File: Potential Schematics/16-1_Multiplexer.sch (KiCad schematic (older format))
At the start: 2 parts, among them U181 74LS04, U194 74LS04

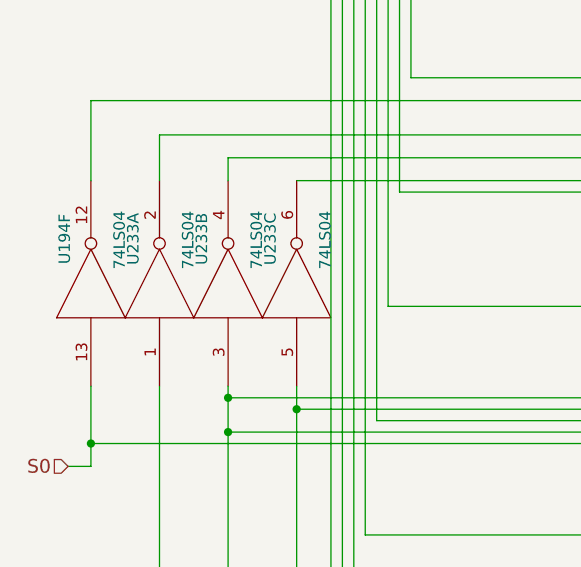
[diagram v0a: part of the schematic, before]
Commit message: Added Registers to Top Schematic
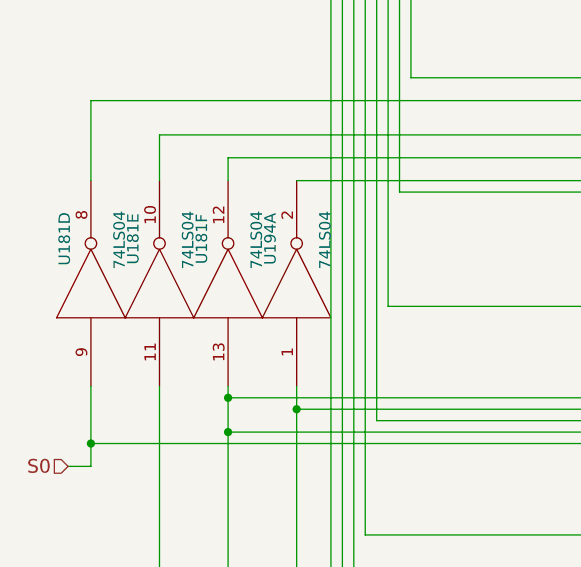
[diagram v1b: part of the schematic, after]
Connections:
- net 5:1_AND/b: now also U194.2; no longer U194.5
- net 5:1_AND/c: now also U181.13; no longer U181.3
- net 5:1_AND/d: now also U181.10; no longer U181.2
- net S0: now also U181.9; no longer U181.13
- net S1: now also U181.11; no longer U181.1
- removed net 5:1_AND/b: U194.6
- removed net 5:1_AND/c: U181.12, U181.4
- new net 5:1_AND/b: U194.1
- new net 5:1_AND/c: U181.12, U181.8
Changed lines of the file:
@@
 $Descr A4 11693 8268
 encoding utf-8
-Sheet 414 449
+Sheet 378 449
 Title "16:1 Multiplexer"
 Date "2018-09-14"
@@
 $Comp
 L 74LS04 U194
-U 3 1 5BB53D19
+U 1 1 5BB53D19
 P 1700 5450
 AR Path="/5B9D167A/5B9C0EA0/5BAE2F4B/5BAE3D50/5BB53D19" Ref="U194"  Part="1"
@@
 AR Path="/5B9D167A/5B9C0EA0/5BAE2F4B/5BC8F4EC/5BB53D19" Ref="U233"  Part="3"
 AR Path="/5B9D167A/5B9C0EA0/5BAE2F4B/5BC8F503/5BB53D19" Ref="U253"  Part="1"
-F 0 "U233" H 1895 5565 50  0000 C CNN
+F 0 "U194" H 1895 5565 50  0000 C CNN
 F 1 "74LS04" H 1890 5325 50  0000 C CNN
 F 2 "" H 1700 5450 50  0001 C CNN
 F 3 "" H 1700 5450 50  0001 C CNN
-	3    1700 5450
+	1    1700 5450
 	0    -1   -1   0
 $EndComp
 $Comp
 L 74LS04 U181
-U 2 1 5BB54417
+U 6 1 5BB54417
 P 1400 5450
 AR Path="/5B9D167A/5B9C0EA0/5BAE2F4B/5BAE3D50/5BB54417" Ref="U181"  Part="6"
@@
 AR Path="/5B9D167A/5B9C0EA0/5BAE2F4B/5BC8F4EC/5BB54417" Ref="U233"  Part="2"
 AR Path="/5B9D167A/5B9C0EA0/5BAE2F4B/5BC8F503/5BB54417" Ref="U233"  Part="6"
-F 0 "U233" H 1595 5565 50  0000 C CNN
+F 0 "U181" H 1595 5565 50  0000 C CNN
 F 1 "74LS04" H 1590 5325 50  0000 C CNN
 F 2 "" H 1400 5450 50  0001 C CNN
 F 3 "" H 1400 5450 50  0001 C CNN
-	2    1400 5450
+	6    1400 5450
 	0    -1   -1   0
 $EndComp
 $Comp
 L 74LS04 U181
-U 1 1 5BB55464
+U 5 1 5BB55464
 P 1100 5450
 AR Path="/5B9D167A/5B9C0EA0/5BAE2F4B/5BAE3D50/5BB55464" Ref="U181"  Part="5"
@@
 AR Path="/5B9D167A/5B9C0EA0/5BAE2F4B/5BC8F4EC/5BB55464" Ref="U233"  Part="1"
 AR Path="/5B9D167A/5B9C0EA0/5BAE2F4B/5BC8F503/5BB55464" Ref="U233"  Part="5"
-F 0 "U233" H 1295 5565 50  0000 C CNN
+F 0 "U181" H 1295 5565 50  0000 C CNN
 F 1 "74LS04" H 1290 5325 50  0000 C CNN
 F 2 "" H 1100 5450 50  0001 C CNN
 F 3 "" H 1100 5450 50  0001 C CNN
-	1    1100 5450
+	5    1100 5450
 	0    -1   -1   0
 $EndComp
 $Comp
 L 74LS04 U181
-U 6 1 5BB5546A
+U 4 1 5BB5546A
 P 800 5450
 AR Path="/5B9D167A/5B9C0EA0/5BAE2F4B/5BAE3D50/5BB5546A" Ref="U181"  Part="4"
@@
 AR Path="/5B9D167A/5B9C0EA0/5BAE2F4B/5BC8F4EC/5BB5546A" Ref="U194"  Part="6"
 AR Path="/5B9D167A/5B9C0EA0/5BAE2F4B/5BC8F503/5BB5546A" Ref="U233"  Part="4"
-F 0 "U194" H 995 5565 50  0000 C CNN
+F 0 "U181" H 995 5565 50  0000 C CNN
 F 1 "74LS04" H 990 5325 50  0000 C CNN
 F 2 "" H 800 5450 50  0001 C CNN
 F 3 "" H 800 5450 50  0001 C CNN
-	6    800  5450
+	4    800  5450
 	0    -1   -1   0
 $EndComp

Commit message: Adding Multiply Devide
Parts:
- U181, U194: symbol 74LS04 -> 4-bit_processor-rescue:74LS04
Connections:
- net 5:1_AND/b is gone; now on net 5:1_AND/b: U194.2
- net 5:1_AND/c is gone; now on net 5:1_AND/c: U181.13
- net 5:1_AND/b: no longer U194.1
- net 5:1_AND/c: no longer U181.12, U181.8
- new net 5:1_AND/b: U194.1
- new net 5:1_AND/c: U181.12, U181.8
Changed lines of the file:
@@
-EESchema Schematic File Version 2
-LIBS:power
-LIBS:device
-LIBS:switches
-LIBS:relays
-LIBS:motors
-LIBS:transistors
-LIBS:conn
-LIBS:linear
-LIBS:regul
-LIBS:74xx
-LIBS:cmos4000
-LIBS:adc-dac
-LIBS:memory
-LIBS:xilinx
-LIBS:microcontrollers
-LIBS:dsp
-LIBS:microchip
-LIBS:analog_switches
-LIBS:motorola
-LIBS:texas
-LIBS:intel
-LIBS:audio
-LIBS:interface
-LIBS:digital-audio
-LIBS:philips
-LIBS:display
-LIBS:cypress
-LIBS:siliconi
-LIBS:opto
-LIBS:atmel
-LIBS:contrib
-LIBS:valves
+EESchema Schematic File Version 4
 LIBS:4-bit_processor-cache
-EELAYER 25 0
+EELAYER 26 0
 EELAYER END
 $Descr A4 11693 8268
 encoding utf-8
-Sheet 378 449
+Sheet 378 451
 Title "16:1 Multiplexer"
 Date "2018-09-14"
@@
 $EndSheet
 $Comp
-L 74LS04 U194
+L 4-bit_processor-rescue:74LS04 U194
 U 1 1 5BB53D19
 P 1700 5450
@@
 $EndComp
 $Comp
-L 74LS04 U181
+L 4-bit_processor-rescue:74LS04 U181
 U 6 1 5BB54417
 P 1400 5450
@@
 $EndComp
 $Comp
-L 74LS04 U181
+L 4-bit_processor-rescue:74LS04 U181
 U 5 1 5BB55464
 P 1100 5450
@@
 $EndComp
 $Comp
-L 74LS04 U181
+L 4-bit_processor-rescue:74LS04 U181
 U 4 1 5BB5546A
 P 800 5450

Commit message: Finished PCB
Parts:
- U195: renamed from U181; footprint (none) -> Daniel_Kopp:DIP-14_300_ELL
- U208: renamed from U194; footprint (none) -> Daniel_Kopp:DIP-14_300_ELL
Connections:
- net 5:1_AND/b is gone; now on net 5:1_AND/b: U208.2
- net 5:1_AND/c is gone; now on net 5:1_AND/c: U195.13
- net 5:1_AND/b: no longer U208.1
- net 5:1_AND/c: no longer U195.12, U195.8
- new net 5:1_AND/b: U208.1
- new net 5:1_AND/c: U195.12, U195.8
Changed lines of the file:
@@
 $Descr A4 11693 8268
 encoding utf-8
-Sheet 378 451
+Sheet 378 456
 Title "16:1 Multiplexer"
 Date "2018-09-14"
@@
 $EndSheet
 $Comp
-L 4-bit_processor-rescue:74LS04 U194
+L 4-bit_processor-rescue:74LS04 U208
 U 1 1 5BB53D19
 P 1700 5450
-AR Path="/5B9D167A/5B9C0EA0/5BAE2F4B/5BAE3D50/5BB53D19" Ref="U194"  Part="1"
-AR Path="/5B9D167A/5B9C0EA0/5BAE2F4B/5BC8C0A9/5BB53D19" Ref="U194"  Part="5"
-AR Path="/5B9D167A/5B9C0EA0/5BAE2F4B/5BC8F4EC/5BB53D19" Ref="U233"  Part="3"
-AR Path="/5B9D167A/5B9C0EA0/5BAE2F4B/5BC8F503/5BB53D19" Ref="U253"  Part="1"
-F 0 "U194" H 1895 5565 50  0000 C CNN
+AR Path="/5B9D167A/5B9C0EA0/5BAE2F4B/5BAE3D50/5BB53D19" Ref="U208"  Part="1"
+AR Path="/5B9D167A/5B9C0EA0/5BAE2F4B/5BC8C0A9/5BB53D19" Ref="U208"  Part="5"
+AR Path="/5B9D167A/5B9C0EA0/5BAE2F4B/5BC8F4EC/5BB53D19" Ref="U248"  Part="3"
+AR Path="/5B9D167A/5B9C0EA0/5BAE2F4B/5BC8F503/5BB53D19" Ref="U269"  Part="1"
+F 0 "U269" H 1895 5565 50  0000 C CNN
 F 1 "74LS04" H 1890 5325 50  0000 C CNN
-F 2 "" H 1700 5450 50  0001 C CNN
+F 2 "Daniel_Kopp:DIP-14_300_ELL" H 1700 5450 50  0001 C CNN
 F 3 "" H 1700 5450 50  0001 C CNN
 	1    1700 5450
@@
 $EndComp
 $Comp
-L 4-bit_processor-rescue:74LS04 U181
+L 4-bit_processor-rescue:74LS04 U195
 U 6 1 5BB54417
 P 1400 5450
-AR Path="/5B9D167A/5B9C0EA0/5BAE2F4B/5BAE3D50/5BB54417" Ref="U181"  Part="6"
-AR Path="/5B9D167A/5B9C0EA0/5BAE2F4B/5BC8C0A9/5BB54417" Ref="U194"  Part="4"
-AR Path="/5B9D167A/5B9C0EA0/5BAE2F4B/5BC8F4EC/5BB54417" Ref="U233"  Part="2"
-AR Path="/5B9D167A/5B9C0EA0/5BAE2F4B/5BC8F503/5BB54417" Ref="U233"  Part="6"
-F 0 "U181" H 1595 5565 50  0000 C CNN
+AR Path="/5B9D167A/5B9C0EA0/5BAE2F4B/5BAE3D50/5BB54417" Ref="U195"  Part="6"
+AR Path="/5B9D167A/5B9C0EA0/5BAE2F4B/5BC8C0A9/5BB54417" Ref="U208"  Part="4"
+AR Path="/5B9D167A/5B9C0EA0/5BAE2F4B/5BC8F4EC/5BB54417" Ref="U248"  Part="2"
+AR Path="/5B9D167A/5B9C0EA0/5BAE2F4B/5BC8F503/5BB54417" Ref="U248"  Part="6"
+F 0 "U248" H 1595 5565 50  0000 C CNN
 F 1 "74LS04" H 1590 5325 50  0000 C CNN
-F 2 "" H 1400 5450 50  0001 C CNN
+F 2 "Daniel_Kopp:DIP-14_300_ELL" H 1400 5450 50  0001 C CNN
 F 3 "" H 1400 5450 50  0001 C CNN
 	6    1400 5450
@@
 $EndComp
 $Comp
-L 4-bit_processor-rescue:74LS04 U181
+L 4-bit_processor-rescue:74LS04 U195
 U 5 1 5BB55464
 P 1100 5450
-AR Path="/5B9D167A/5B9C0EA0/5BAE2F4B/5BAE3D50/5BB55464" Ref="U181"  Part="5"
-AR Path="/5B9D167A/5B9C0EA0/5BAE2F4B/5BC8C0A9/5BB55464" Ref="U194"  Part="3"
-AR Path="/5B9D167A/5B9C0EA0/5BAE2F4B/5BC8F4EC/5BB55464" Ref="U233"  Part="1"
-AR Path="/5B9D167A/5B9C0EA0/5BAE2F4B/5BC8F503/5BB55464" Ref="U233"  Part="5"
-F 0 "U181" H 1295 5565 50  0000 C CNN
+AR Path="/5B9D167A/5B9C0EA0/5BAE2F4B/5BAE3D50/5BB55464" Ref="U195"  Part="5"
+AR Path="/5B9D167A/5B9C0EA0/5BAE2F4B/5BC8C0A9/5BB55464" Ref="U208"  Part="3"
+AR Path="/5B9D167A/5B9C0EA0/5BAE2F4B/5BC8F4EC/5BB55464" Ref="U248"  Part="1"
+AR Path="/5B9D167A/5B9C0EA0/5BAE2F4B/5BC8F503/5BB55464" Ref="U248"  Part="5"
+F 0 "U248" H 1295 5565 50  0000 C CNN
 F 1 "74LS04" H 1290 5325 50  0000 C CNN
-F 2 "" H 1100 5450 50  0001 C CNN
+F 2 "Daniel_Kopp:DIP-14_300_ELL" H 1100 5450 50  0001 C CNN
 F 3 "" H 1100 5450 50  0001 C CNN
 	5    1100 5450
@@
 $EndComp
 $Comp
-L 4-bit_processor-rescue:74LS04 U181
+L 4-bit_processor-rescue:74LS04 U195
 U 4 1 5BB5546A
 P 800 5450
-AR Path="/5B9D167A/5B9C0EA0/5BAE2F4B/5BAE3D50/5BB5546A" Ref="U181"  Part="4"
-AR Path="/5B9D167A/5B9C0EA0/5BAE2F4B/5BC8C0A9/5BB5546A" Ref="U194"  Part="2"
-AR Path="/5B9D167A/5B9C0EA0/5BAE2F4B/5BC8F4EC/5BB5546A" Ref="U194"  Part="6"
-AR Path="/5B9D167A/5B9C0EA0/5BAE2F4B/5BC8F503/5BB5546A" Ref="U233"  Part="4"
-F 0 "U181" H 995 5565 50  0000 C CNN
+AR Path="/5B9D167A/5B9C0EA0/5BAE2F4B/5BAE3D50/5BB5546A" Ref="U195"  Part="4"
+AR Path="/5B9D167A/5B9C0EA0/5BAE2F4B/5BC8C0A9/5BB5546A" Ref="U208"  Part="2"
+AR Path="/5B9D167A/5B9C0EA0/5BAE2F4B/5BC8F4EC/5BB5546A" Ref="U208"  Part="6"
+AR Path="/5B9D167A/5B9C0EA0/5BAE2F4B/5BC8F503/5BB5546A" Ref="U248"  Part="4"
+F 0 "U248" H 995 5565 50  0000 C CNN
 F 1 "74LS04" H 990 5325 50  0000 C CNN
-F 2 "" H 800 5450 50  0001 C CNN
+F 2 "Daniel_Kopp:DIP-14_300_ELL" H 800 5450 50  0001 C CNN
 F 3 "" H 800 5450 50  0001 C CNN
 	4    800  5450
@@
 	700  6250 800  6250
 Wire Wire Line
-	800  6250 800  5900
+	800  6250 800  6150
 Wire Wire Line
 	700  6750 1100 6750
@@
 	750  7250 1400 7250
 Wire Wire Line
-	1400 7250 1400 5900
+	1400 7250 1400 6100
 Wire Wire Line
 	750  7750 1700 7750
 Wire Wire Line
-	1700 7750 1700 5900
+	1700 7750 1700 6000
 Wire Wire Line
 	1700 5000 3900 5000
 Wire Wire Line
-	3900 5000 3900 650
+	3900 5000 3900 4150
 Wire Wire Line
 	3900 650  4050 650
@@
 	1400 5000 1400 4900
 Wire Wire Line
-	1400 4900 3850 4900
-Wire Wire Line
-	3850 750  3850 6250
+	1400 4900 3750 4900
+Wire Wire Line
+	3850 750  3850 1250
 Wire Wire Line
 	3850 750  4050 750
@@
 	1100 4800 3800 4800
 Wire Wire Line
-	3800 850  3800 4850
+	3800 850  3800 1350
 Wire Wire Line
 	3800 850  4050 850
@@
 	800  4650 3750 4650
 Wire Wire Line
-	3750 950  3750 4950
+	3750 950  3750 1950
 Wire Wire Line
 	3750 950  4050 950
@@
 	4050 5350 3800 5350
 Wire Wire Line
-	3800 4800 3800 7250
+	3800 4800 3800 4850
 Wire Wire Line
 	3800 4850 4050 4850
@@
 	4050 5950 3750 5950
 Wire Wire Line
-	3750 4900 3750 7200
+	3750 4900 3750 4950
 Connection ~ 3750 4900
 Wire Wire Line
@@
 	1700 6000 3700 6000
 Wire Wire Line
-	3700 4700 3700 7350
+	3700 4700 3700 5150
 Wire Wire Line
 	3700 4700 4000 4700
@@
 	5950 6400 5350 6400
 Wire Wire Line
-	3700 7350 5900 7350
+	3700 7350 5350 7350
 Connection ~ 3700 6650
 Wire Wire Line
 	5950 6900 5350 6900
-Wire Wire Line
-	5350 6900 5350 6950
-Connection ~ 5350 6950
 Connection ~ 5350 7350
 Wire Wire Line
-	5350 6400 5350 7350
-Wire Wire Line
 	5900 7350 5900 7400
 Wire Wire Line
@@
 Wire Wire Line
 	1400 5950 3650 5950
-Wire Wire Line
-	3650 2750 3650 7400
 Wire Wire Line
 	3650 2750 4050 2750
@@
 Wire Wire Line
 	4050 3250 3650 3250
-Wire Wire Line
-	3650 3250 3650 3200
 Connection ~ 3650 3200
 Wire Wire Line
@@
 Connection ~ 3650 5950
 Wire Wire Line
-	3650 7400 5850 7400
-Wire Wire Line
-	5400 7400 5400 6500
+	3650 7400 5400 7400
+Wire Wire Line
+	5400 7400 5400 7000
 Wire Wire Line
 	5400 6500 5950 6500
@@
 	1400 6100 3600 6100
 Wire Wire Line
-	3600 1850 3600 7450
+	3600 1850 3600 2350
 Wire Wire Line
 	3600 1850 4050 1850
@@
 Connection ~ 3600 6100
 Wire Wire Line
-	3600 7450 5800 7450
+	3600 7450 5450 7450
 Wire Wire Line
 	5450 7450 5450 7100
@@
 	800  6150 3550 6150
 Wire Wire Line
-	3550 1450 3550 7500
+	3550 1450 3550 2450
 Wire Wire Line
 	3550 1450 4050 1450
@@
 	3550 7500 5500 7500
 Wire Wire Line
-	5500 6700 5500 7700
+	5500 6700 5500 7500
 Wire Wire Line
 	5500 7700 5950 7700
@@
 Text Notes 6300 7500 2    60   ~ 0
 AND
+Wire Wire Line
+	3750 1950 3750 2950
+Wire Wire Line
+	3900 1150 3900 650
+Wire Wire Line
+	3850 1250 3850 1750
+Wire Wire Line
+	3800 1350 3800 2850
+Wire Wire Line
+	3900 1650 3900 1150
+Wire Wire Line
+	3850 1750 3850 2250
+Wire Wire Line
+	3850 2250 3850 4750
+Wire Wire Line
+	3900 2150 3900 1650
+Wire Wire Line
+	3900 2650 3900 2150
+Wire Wire Line
+	3750 2950 3750 3950
+Wire Wire Line
+	3800 3350 3800 4800
+Wire Wire Line
+	3800 2850 3800 3350
+Wire Wire Line
+	3900 3150 3900 2650
+Wire Wire Line
+	3750 3950 3750 4650
+Wire Wire Line
+	3900 3650 3900 3150
+Wire Wire Line
+	3900 4150 3900 3650
+Wire Wire Line
+	3850 4750 3850 4900
+Wire Wire Line
+	3750 4650 3750 4900
+Wire Wire Line
+	3850 4900 3850 5250
+Wire Wire Line
+	3800 4850 3800 5350
+Wire Wire Line
+	3850 5250 3850 5750
+Wire Wire Line
+	3750 4900 3850 4900
+Wire Wire Line
+	3750 4950 3750 5950
+Wire Wire Line
+	3800 5350 3800 6850
+Wire Wire Line
+	3750 5950 3750 6950
+Wire Wire Line
+	3850 5750 3850 6250
+Wire Wire Line
+	3750 6950 3750 7200
+Wire Wire Line
+	3800 6850 3800 7250
+Wire Wire Line
+	1700 6000 1700 5900
+Wire Wire Line
+	3700 5150 3700 5650
+Wire Wire Line
+	3700 5650 3700 6000
+Wire Wire Line
+	3700 6000 3700 6150
+Wire Wire Line
+	3700 6150 3700 6650
+Wire Wire Line
+	3700 6650 3700 7350
+Wire Wire Line
+	5350 7350 5900 7350
+Wire Wire Line
+	1400 5950 1400 5900
+Wire Wire Line
+	3650 3750 3650 4250
+Wire Wire Line
+	3650 4250 3650 5950
+Wire Wire Line
+	3650 5950 3650 6750
+Wire Wire Line
+	3650 6750 3650 7400
+Wire Wire Line
+	5400 7000 5400 6500
+Wire Wire Line
+	5400 7400 5850 7400
+Wire Wire Line
+	1400 6100 1400 5950
+Wire Wire Line
+	3600 2350 3600 3850
+Wire Wire Line
+	3600 3850 3600 4350
+Wire Wire Line
+	3600 4350 3600 5850
+Wire Wire Line
+	3600 5850 3600 6100
+Wire Wire Line
+	3600 6100 3600 6350
+Wire Wire Line
+	3600 6350 3600 7450
+Wire Wire Line
+	5450 7450 5800 7450
+Wire Wire Line
+	800  6150 800  5900
+Wire Wire Line
+	3550 2450 3550 3450
+Wire Wire Line
+	3550 3450 3550 4450
+Wire Wire Line
+	3550 4450 3550 5450
+Wire Wire Line
+	3550 5450 3550 6150
+Wire Wire Line
+	3550 6150 3550 6450
+Wire Wire Line
+	3550 6450 3550 7500
+Wire Wire Line
+	5500 7500 5500 7700
+Wire Wire Line
+	5350 6400 5350 7350
+Wire Wire Line
+	3650 2750 3650 3750
 $EndSCHEMATC

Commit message: Working on Multiplier
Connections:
- net 5:1_AND/b is gone; now on net 5:1_AND/b: U208.2
- net 5:1_AND/c is gone; now on net 5:1_AND/c: U195.13
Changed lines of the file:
@@
 $Descr A4 11693 8268
 encoding utf-8
-Sheet 378 456
+Sheet 378 458
 Title "16:1 Multiplexer"
 Date "2018-09-14"

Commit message: Made Multiplier
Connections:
- net 5:1_AND/b is gone; now on net 5:1_AND/b: U208.2
- net 5:1_AND/c is gone; now on net 5:1_AND/c: U195.13
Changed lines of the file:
@@
 $Descr A4 11693 8268
 encoding utf-8
-Sheet 378 458
+Sheet 378 467
 Title "16:1 Multiplexer"
 Date "2018-09-14"

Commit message: Updated overview of Schematic
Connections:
- net 5:1_AND/b is gone; now on net 5:1_AND/b: U208.2
- net 5:1_AND/c is gone; now on net 5:1_AND/c: U195.13
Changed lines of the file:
@@
 $Descr A4 11693 8268
 encoding utf-8
-Sheet 378 467
+Sheet 378 902
 Title "16:1 Multiplexer"
 Date "2018-09-14"

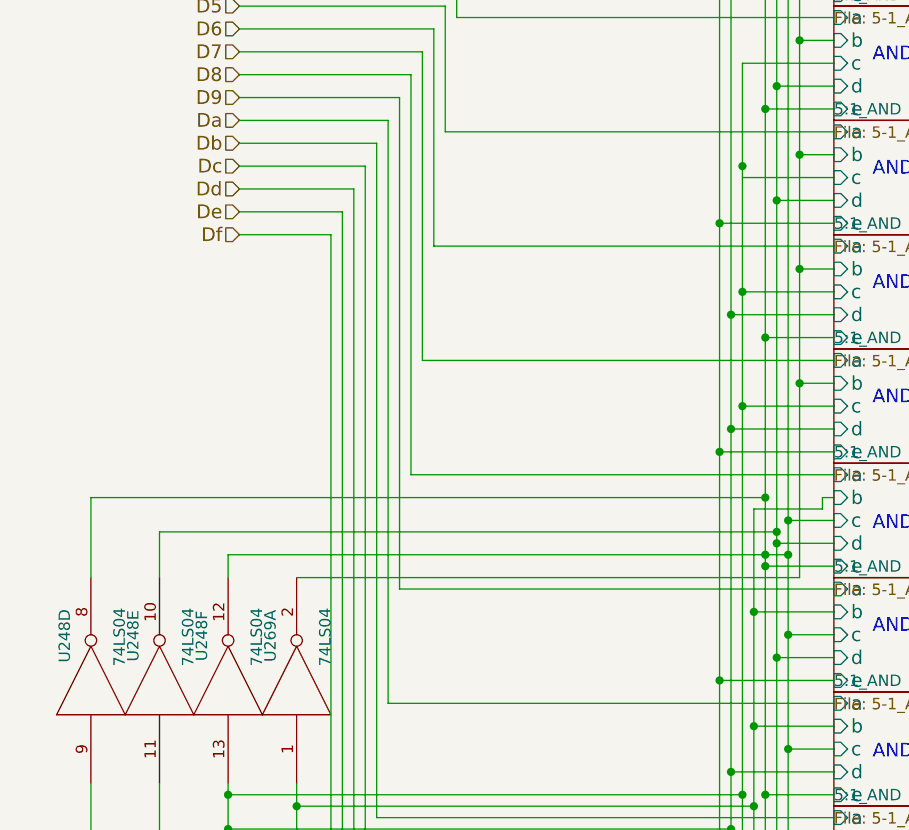
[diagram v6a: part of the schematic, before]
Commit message: In the middle of adding ROM
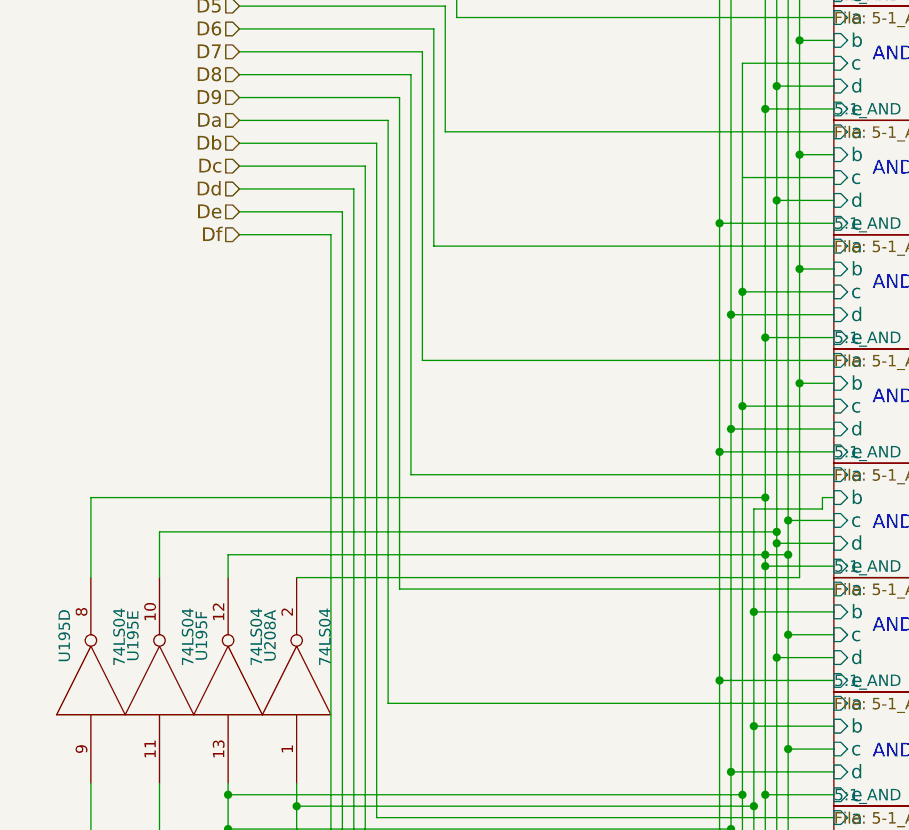
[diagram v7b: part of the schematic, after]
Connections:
- net 5:1_AND/b is gone; now on net 5:1_AND/b: U208.2
- net 5:1_AND/c is gone; now on net 5:1_AND/c: U195.13
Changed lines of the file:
@@
 $Descr A4 11693 8268
 encoding utf-8
-Sheet 378 902
+Sheet 378 1330
 Title "16:1 Multiplexer"
 Date "2018-09-14"
@@
 AR Path="/5B9D167A/5B9C0EA0/5BAE2F4B/5BC8F4EC/5BB53D19" Ref="U248"  Part="3"
 AR Path="/5B9D167A/5B9C0EA0/5BAE2F4B/5BC8F503/5BB53D19" Ref="U269"  Part="1"
-F 0 "U269" H 1895 5565 50  0000 C CNN
+F 0 "U208" H 1895 5565 50  0000 C CNN
 F 1 "74LS04" H 1890 5325 50  0000 C CNN
 F 2 "Daniel_Kopp:DIP-14_300_ELL" H 1700 5450 50  0001 C CNN
@@
 AR Path="/5B9D167A/5B9C0EA0/5BAE2F4B/5BC8F4EC/5BB54417" Ref="U248"  Part="2"
 AR Path="/5B9D167A/5B9C0EA0/5BAE2F4B/5BC8F503/5BB54417" Ref="U248"  Part="6"
-F 0 "U248" H 1595 5565 50  0000 C CNN
+F 0 "U195" H 1595 5565 50  0000 C CNN
 F 1 "74LS04" H 1590 5325 50  0000 C CNN
 F 2 "Daniel_Kopp:DIP-14_300_ELL" H 1400 5450 50  0001 C CNN
@@
 AR Path="/5B9D167A/5B9C0EA0/5BAE2F4B/5BC8F4EC/5BB55464" Ref="U248"  Part="1"
 AR Path="/5B9D167A/5B9C0EA0/5BAE2F4B/5BC8F503/5BB55464" Ref="U248"  Part="5"
-F 0 "U248" H 1295 5565 50  0000 C CNN
+F 0 "U195" H 1295 5565 50  0000 C CNN
 F 1 "74LS04" H 1290 5325 50  0000 C CNN
 F 2 "Daniel_Kopp:DIP-14_300_ELL" H 1100 5450 50  0001 C CNN
@@
 AR Path="/5B9D167A/5B9C0EA0/5BAE2F4B/5BC8F4EC/5BB5546A" Ref="U208"  Part="6"
 AR Path="/5B9D167A/5B9C0EA0/5BAE2F4B/5BC8F503/5BB5546A" Ref="U248"  Part="4"
-F 0 "U248" H 995 5565 50  0000 C CNN
+F 0 "U195" H 995 5565 50  0000 C CNN
 F 1 "74LS04" H 990 5325 50  0000 C CNN
 F 2 "Daniel_Kopp:DIP-14_300_ELL" H 800 5450 50  0001 C CNN
@@
 Wire Wire Line
 	4050 3250 3650 3250
-Connection ~ 3650 3200
 Wire Wire Line
 	4050 3750 3650 3750
